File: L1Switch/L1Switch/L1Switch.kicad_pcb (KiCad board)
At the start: 4 copper layers, 219 parts, among them J1 RJSNEGF8A08, J2 Conn_01x07_Male, J3 Barrel_Jack, T1 SM51589PEL, T2 SM51589PEL, T3 SM51589PEL, T4 SM51589PEL, T5 SM51589PEL, T6 SM51589PEL, T7 SM51589PEL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

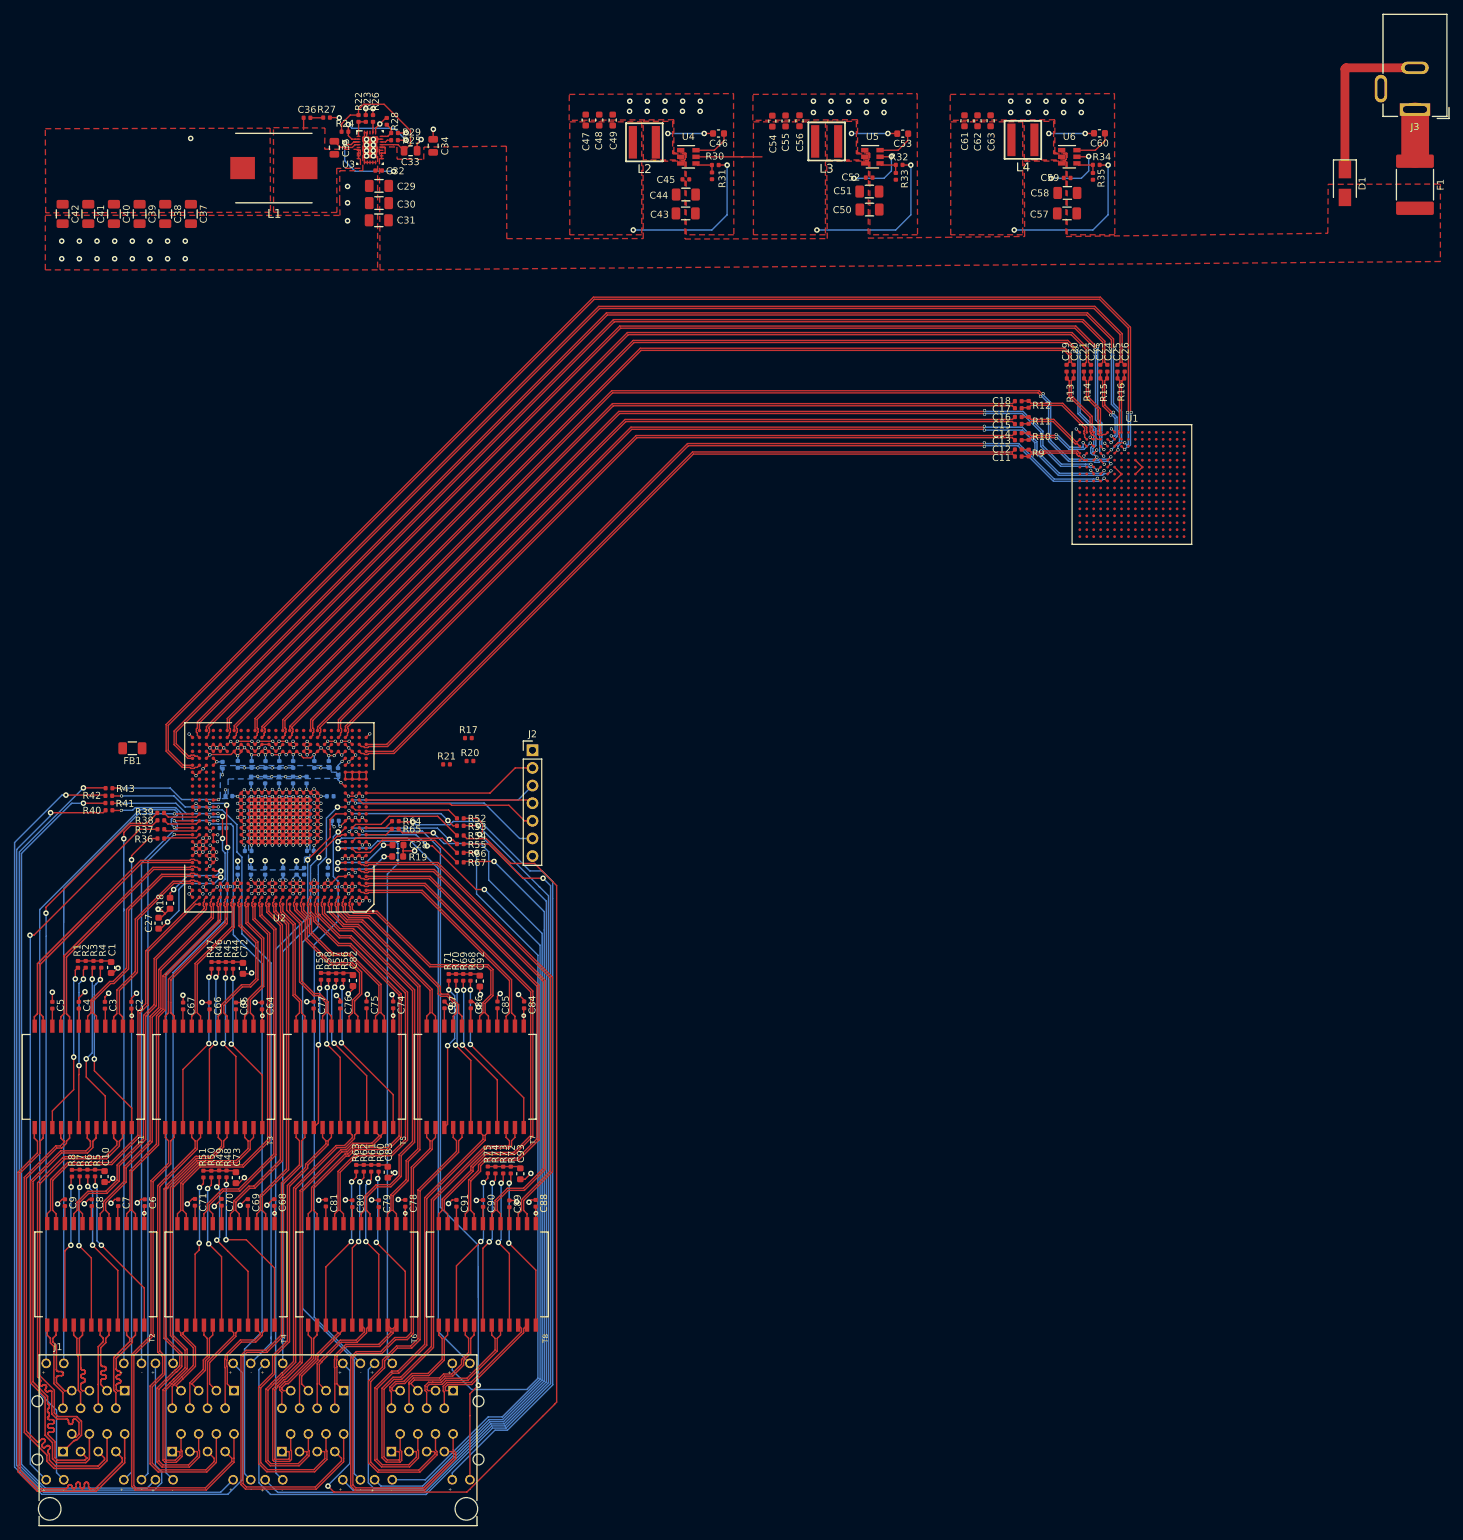
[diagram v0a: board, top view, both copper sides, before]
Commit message: Length match some pairs.
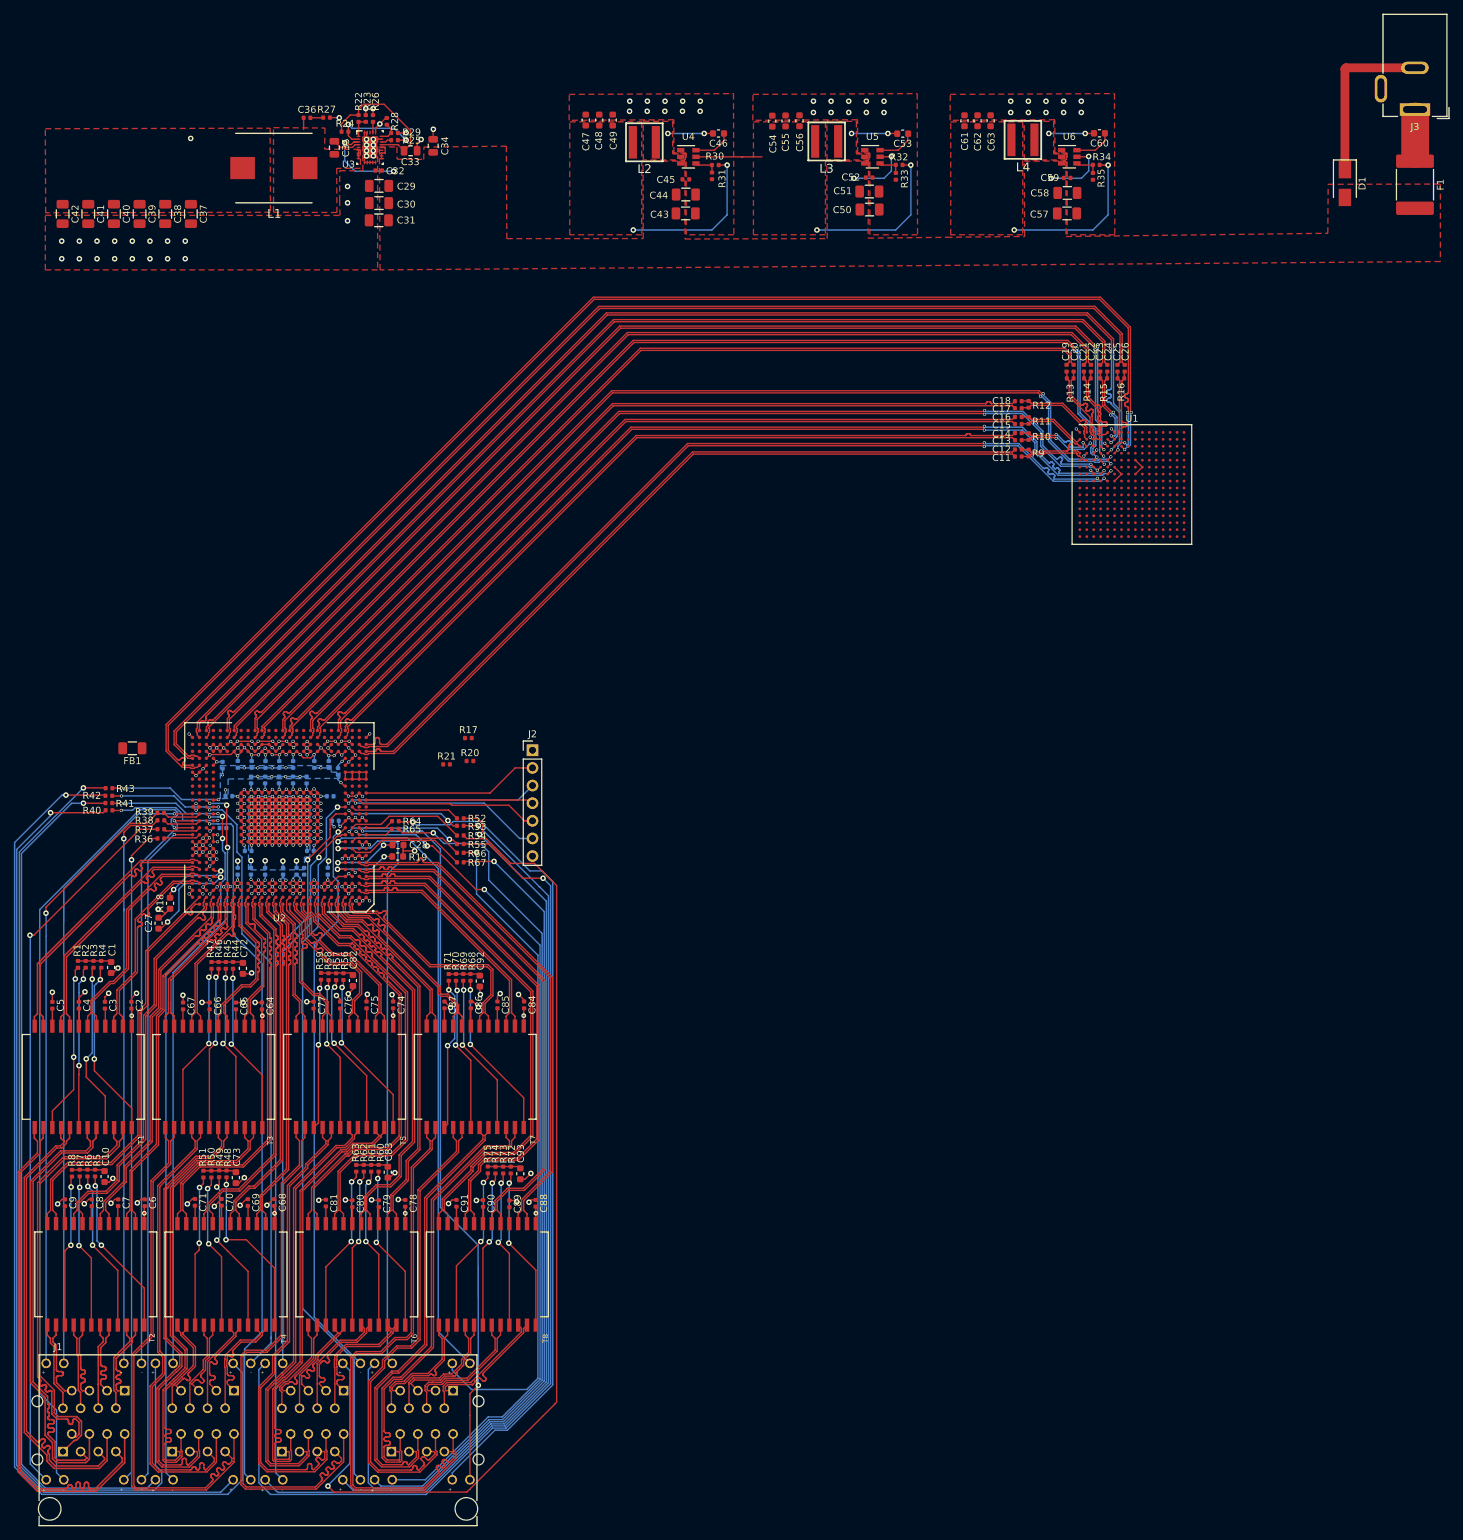
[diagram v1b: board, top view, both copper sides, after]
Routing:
- net /Net 1/P3.D+: track 71.6 -> 74.7 mm
- net /Net 1/P5.D+: track 74.3 -> 77.4 mm
- net /Net 1/P7.A+: track 62.5 -> 65.1 mm
- net /Net 1/P3.A+: track 62.2 -> 64.7 mm
- net /Net 1/P5.C+: track 64.8 -> 67.4 mm
- net /Net 1/P5.A+: track 60.6 -> 63.2 mm
- net /Net 1/P7.D+: track 78.0 -> 80.5 mm
- net /SGMII.TD_N7: track 126.1 -> 128.6 mm
- net /SGMII.TD_N0: track 192.5 -> 194.9 mm
- net /Net 1/P7.C+: track 66.9 -> 69.2 mm
- net /Net 1/P6.B+: track 14.2 -> 16.3 mm
- net /Net 1/P4.B+: track 11.6 -> 13.7 mm
- net /Net 1/P6.C+: track 12.3 -> 14.5 mm
- net /Net 1/P4.A+: track 13.4 -> 15.5 mm
- net /Net 1/P3.C+: track 63.4 -> 65.4 mm
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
